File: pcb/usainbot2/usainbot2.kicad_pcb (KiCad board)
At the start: 2 copper layers, 157 x 131.5 mm, 21 parts, among them J1 BT_MOD, J2 QTR1-L, J3 QTR1-R, J4 QTR-6A, J5 M1, J6 BATT, J7 M2, SW1 SW_SPDT, SW2 SW_Push, U1 TB6612FNG_breakout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

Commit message: updated pcb silkscreen and v3 firmware
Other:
- board text added: "Diseñado para BRC 2022 por Gonzalo O. y Victor C."
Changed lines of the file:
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@@
     (aux_axis_origin 98.425 106.299)
     (pcbplotparams
-      (layerselection 0x0001030_ffffffff)
+      (layerselection 0x00010f0_ffffffff)
       (disableapertmacros false)
       (usegerberextensions false)
@@
     (fp_line (start 13.97 2.88) (end 13.97 -2.92) (layer "F.Fab") (width 0.1))
     (fp_line (start -1.27 -0.5) (end -0.562893 0) (layer "F.Fab") (width 0.1))
-    (pad "1" thru_hole roundrect (at 0 0 90) (size 1.74 2.19) (drill 1.19) (layers *.Cu *.Mask) (roundrect_rratio 0.143678)
+    (pad "1" thru_hole roundrect (at 0 0 90) (size 1.74 2.19) (drill 1.19) (layers *.Cu *.Mask) (roundrect_rratio 0.1436781609)
       (net 18 "/ML-1") (pinfunction "Pin_1") (pintype "passive"))
     (pad "2" thru_hole oval (at 2.54 0 90) (size 1.74 2.19) (drill 1.19) (layers *.Cu *.Mask)
@@
     (fp_line (start 13.97 2.88) (end 13.97 -2.92) (layer "F.Fab") (width 0.1))
     (fp_line (start -1.27 -2.92) (end -1.27 2.88) (layer "F.Fab") (width 0.1))
-    (pad "1" thru_hole roundrect (at 0 0 270) (size 1.74 2.19) (drill 1.19) (layers *.Cu *.Mask) (roundrect_rratio 0.143678)
+    (pad "1" thru_hole roundrect (at 0 0 270) (size 1.74 2.19) (drill 1.19) (layers *.Cu *.Mask) (roundrect_rratio 0.1436781609)
       (net 29 "/MR-1") (pinfunction "Pin_1") (pintype "passive"))
     (pad "2" thru_hole oval (at 2.54 0 270) (size 1.74 2.19) (drill 1.19) (layers *.Cu *.Mask)
@@
   (gr_line (start 128.397317 109.289112) (end 123.659815 92.707852) (layer "Edge.Cuts") (width 0.2))
   (gr_arc (start 43.370599 128.695599) (mid 43.953593 127.284217) (end 45.362654 126.695615) (layer "Edge.Cuts") (width 0.2))
+  (gr_text "Diseñado para BRC 2022\npor Gonzalo O. y Victor C." (at 99.06 46.99) (layer "B.SilkS")
+    (effects (font (size 1.5 1.5) (thickness 0.3)) (justify mirror))
+  )
   (dimension (type aligned) (layer "Dwgs.User")
     (pts (xy 113.792 106.807) (xy 98.425 106.807))

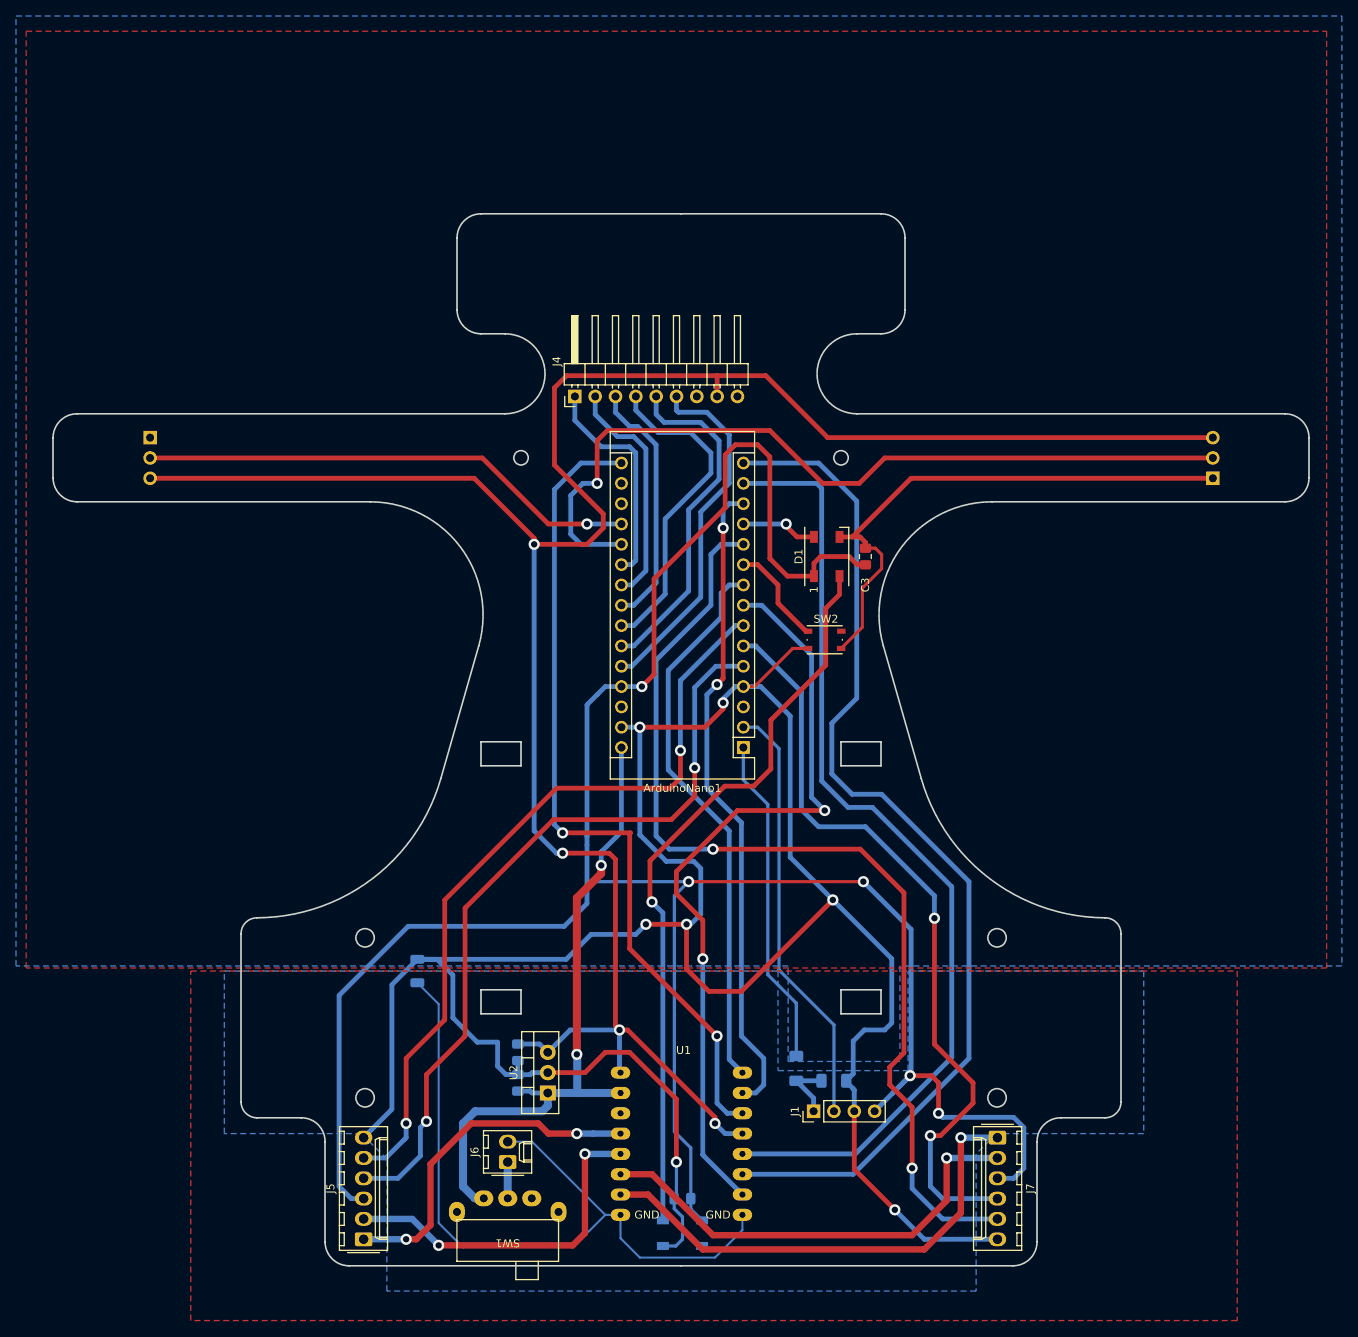
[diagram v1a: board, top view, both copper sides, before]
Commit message: add TB6612FNG documentation and update pcb
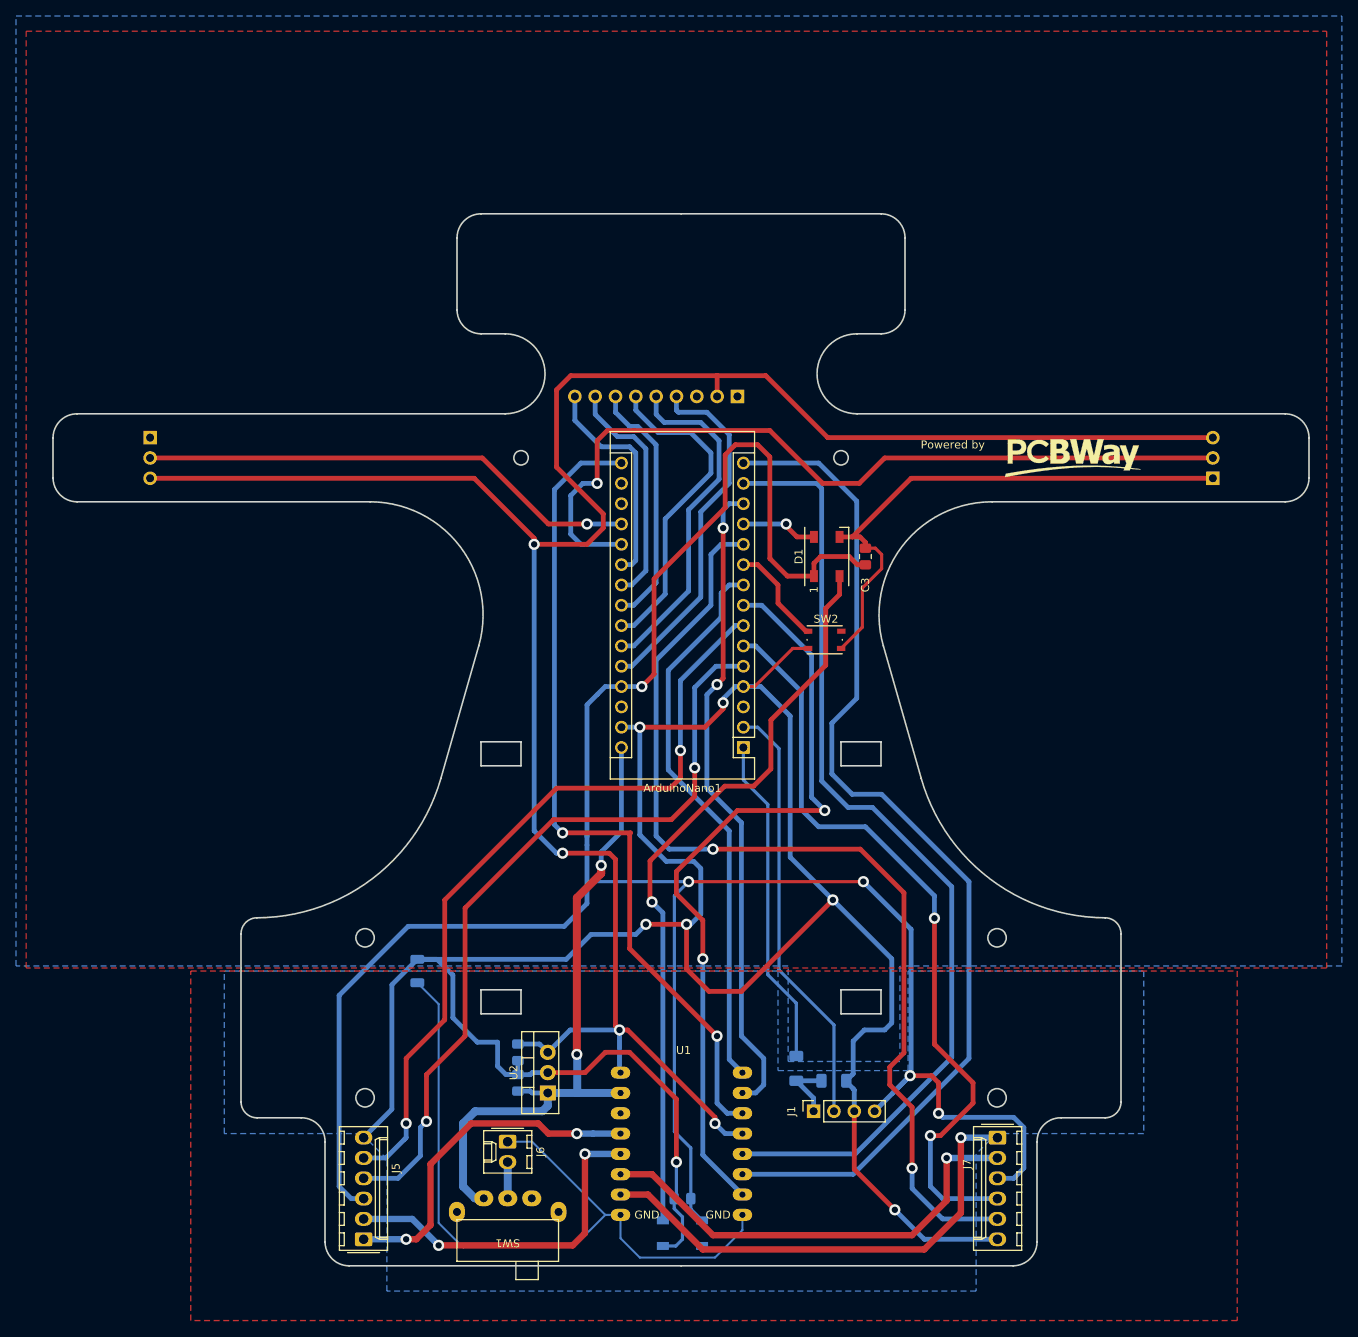
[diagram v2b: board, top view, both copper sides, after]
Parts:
- J1: footprint Connector_PinHeader_2.54mm:PinHeader_1x04_P2.54mm_Vertical -> Connector_PinSocket_2.54mm:PinSocket_1x04_P2.54mm_Vertical
- J2, J3: footprint Connector_PinHeader_2.54mm:PinHeader_1x03_P2.54mm_Horizontal -> Connector_PinHeader_2.54mm:PinHeader_1x03_P2.54mm_Vertical
- J4: moved to B.Cu
- moved J4 20.3 mm to (105.4, 61.5)
- moved J6 2.54 mm to (76.7, 154.7), turned to -90 degrees
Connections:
- J4 pad 1: Net-(ArduinoNano1-Pad21) -> GND
- J4 pad 2: Net-(ArduinoNano1-Pad22) -> +5V
- J4 pad 3: Net-(ArduinoNano1-Pad23) -> unconnected-(J4-Pad3)
- J4 pad 4: Net-(ArduinoNano1-Pad24) -> Net-(ArduinoNano1-Pad26)
- J4 pad 6: Net-(ArduinoNano1-Pad26) -> Net-(ArduinoNano1-Pad24)
- J4 pad 7: unconnected-(J4-Pad7) -> Net-(ArduinoNano1-Pad23)
- J4 pad 8: +5V -> Net-(ArduinoNano1-Pad22)
- J4 pad 9: GND -> Net-(ArduinoNano1-Pad21)
- J6 pad 1: Net-(J6-Pad1) -> GNDPWR
- J6 pad 2: GNDPWR -> Net-(J6-Pad2)
- SW1 pad 2: Net-(J6-Pad1) -> Net-(J6-Pad2)
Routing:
- net Net-(J6-Pad2): track 0.00 -> 4.59 mm
- net Net-(J6-Pad1): track 4.59 -> 0.00 mm
- net +5V: track 280.0 -> 279.5 mm
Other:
- board text added: "Powered by"
